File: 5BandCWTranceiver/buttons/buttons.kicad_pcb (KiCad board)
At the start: 2 copper layers, 78.7 x 27.9 mm, 8 parts, among them J1 Conn_01x04_Female, SW1 SW_Push, SW2 SW_Push, SW3 SW_Push

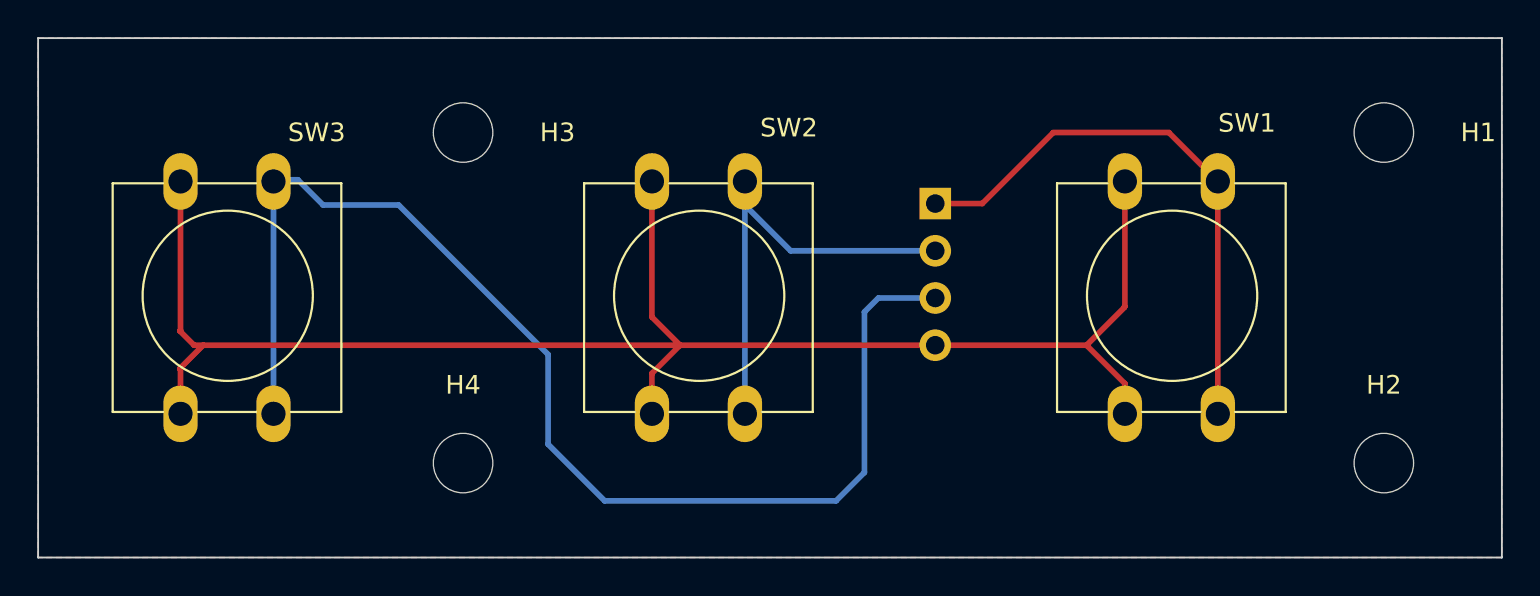
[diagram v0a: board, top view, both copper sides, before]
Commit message: Board Tape Out
Final tapeout changes; board ordered
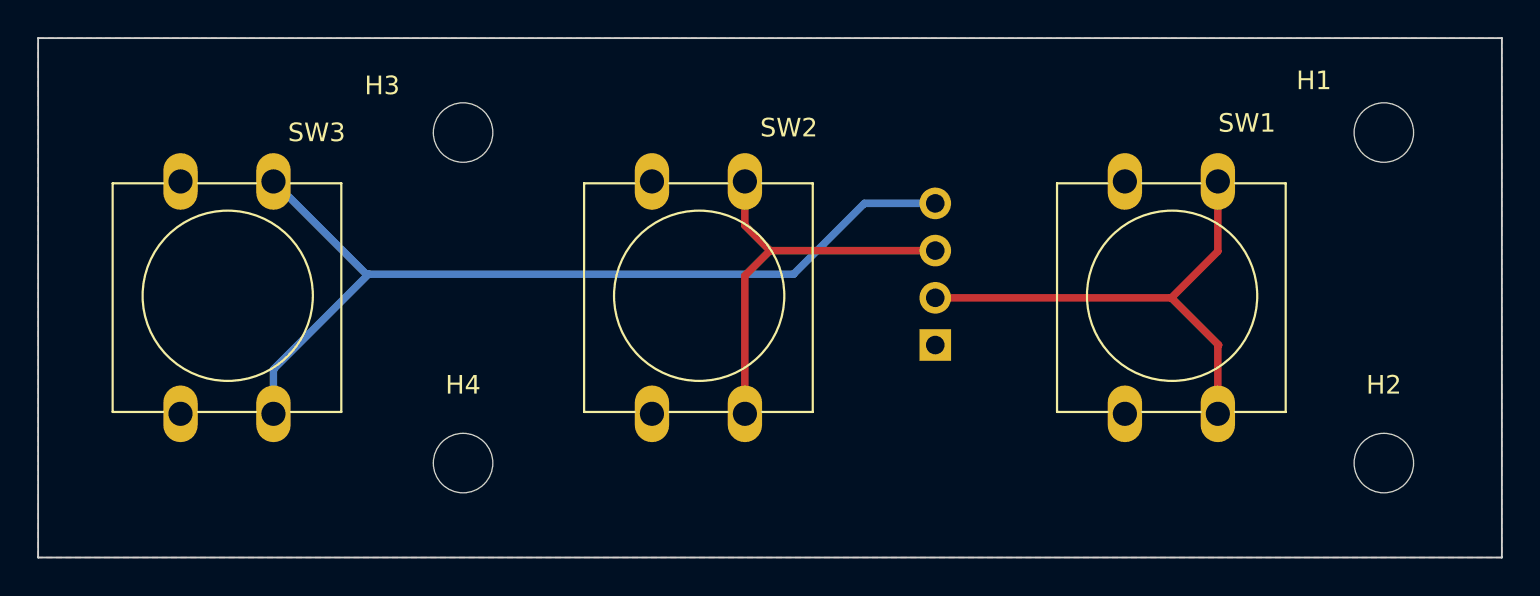
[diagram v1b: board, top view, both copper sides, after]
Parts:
- moved J1 7.61 mm to (167.6, 82.5), turned to 0 degrees
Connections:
- J1 pad 1: /B1 -> GND
- J1 pad 2: /B2 -> /B1
- J1 pad 3: /B3 -> /B2
- J1 pad 4: GND -> /B3
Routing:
- net GND: track 89.3 -> 0.00 mm
- net /B3: track 67.7 -> 48.9 mm
- net /B1: track 31.5 -> 27.3 mm
- net /B2: track 25.0 -> 22.5 mm
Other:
- board text added: "-"
- board text added: "BAND"
- board text added: "DIGIT"
- board text added: "FILTER"
- board text added: "GND"
- board text added: "MENU"
- board text added: "MODE"
- board text added: "MUTE"
- board text added: "N7WMN 5 Band Tranceiver Button Board"
- board text added: "SPOT"
- board text added: "TX"
